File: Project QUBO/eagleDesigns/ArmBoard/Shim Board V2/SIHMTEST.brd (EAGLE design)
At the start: 71.1 x 81.3 mm, 30 parts, among them IC1 MCP2551/SN, U1 BME280

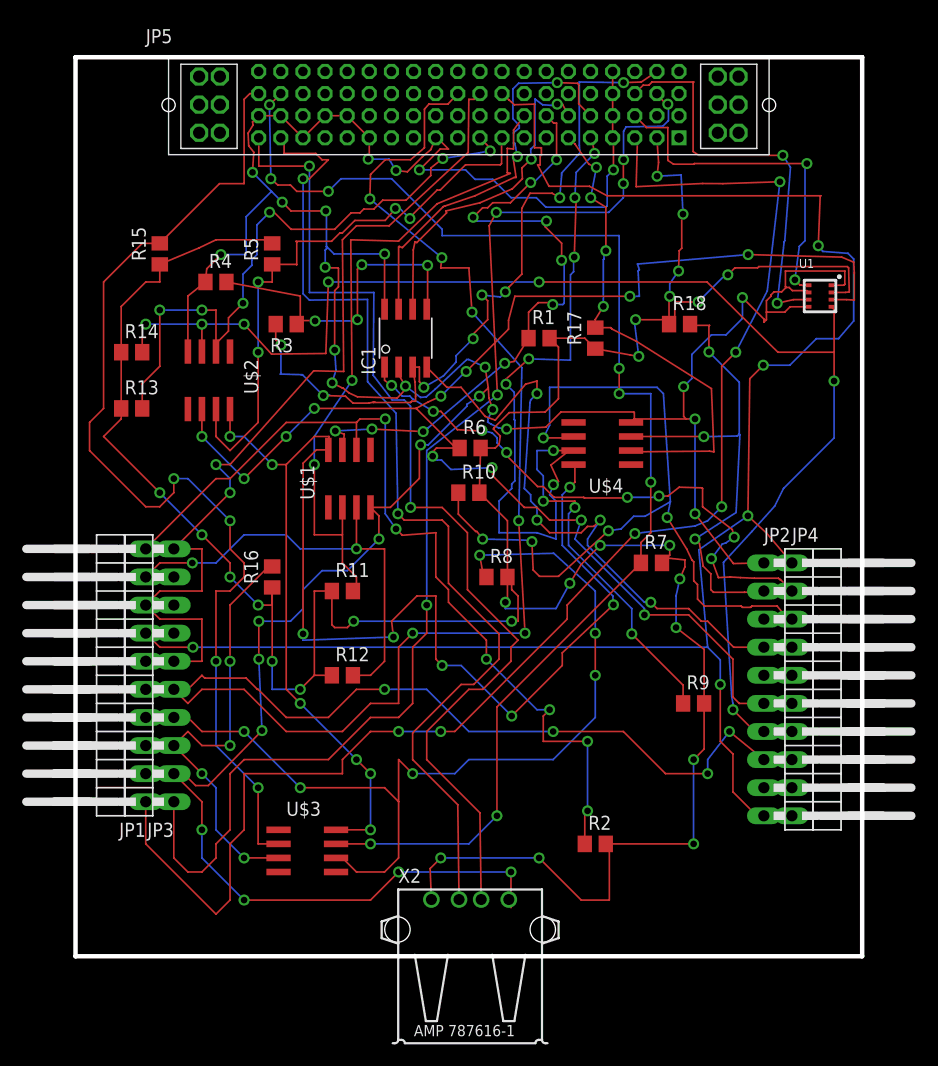
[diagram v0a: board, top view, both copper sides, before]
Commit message: 
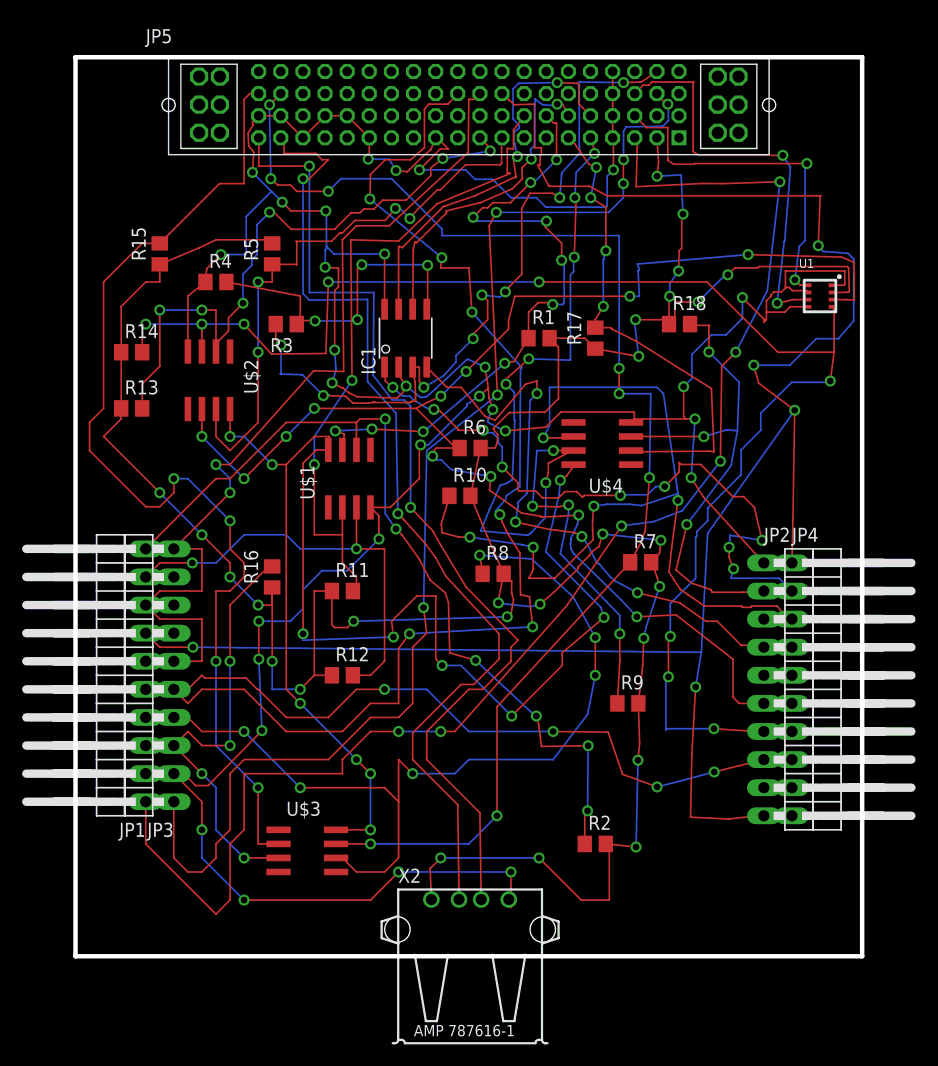
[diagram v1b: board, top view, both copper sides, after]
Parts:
- moved R9 5.94 mm to (49.9, 22.9)
- moved R7 0.97 mm to (51.1, 35.6)
- moved R10 0.85 mm to (34.8, 41.6)
- moved R8 0.45 mm to (37.8, 34.6)
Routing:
- net SPI_CLK: track 163.7 -> 177.7 mm
- net UNBUFFERSCL1: track 121.5 -> 132.8 mm, vias 7 -> 9
- net 5.0(BME): track 275.5 -> 265.0 mm
- net CANTX: track 52.5 -> 60.5 mm, vias 8 -> 9
- net UNBUFFERSDA3: track 74.3 -> 80.2 mm
- net UNBUFFERSDA2: track 84.8 -> 81.9 mm
- net BUFFERSDA3: track 91.4 -> 88.6 mm
- net UNBUFFERSDA0: track 80.5 -> 78.0 mm
- net CANRX: track 55.9 -> 53.5 mm
- net USB-: track 91.9 -> 89.5 mm
- net USB+: track 93.0 -> 90.9 mm
- net 3.3(1): track 129.2 -> 127.3 mm
- net GND: track 315.9 -> 314.4 mm
- net UNBUFFERSCL3: track 44.1 -> 44.9 mm
- net MISO: track 165.9 -> 166.7 mm
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
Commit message: 
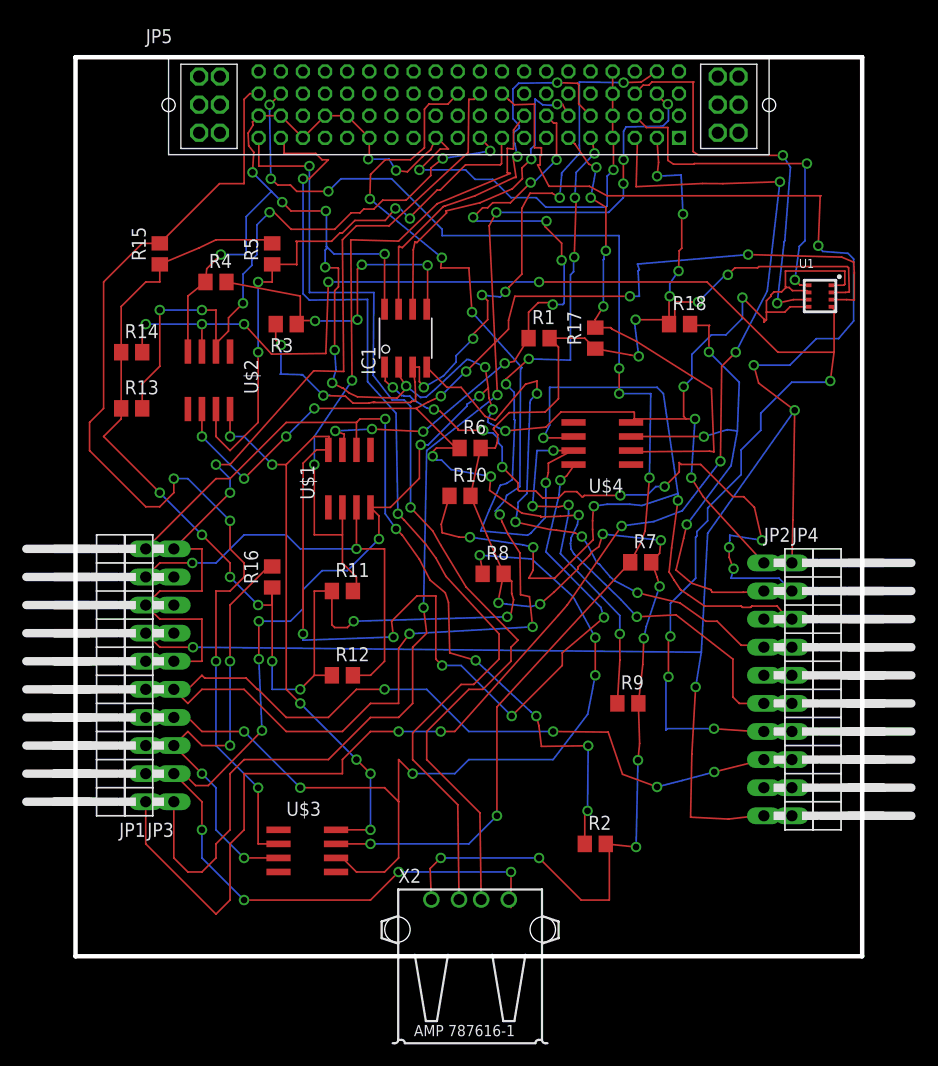
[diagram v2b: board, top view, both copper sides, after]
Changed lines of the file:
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@@
 </class>
 </classes>
-<designrules name="typical_4pcb">
+<designrules name="OshPark">
 <description language="de">&lt;b&gt;EAGLE Design Rules&lt;/b&gt;
 &lt;p&gt;
@@
 Einstellungen hier und speichern die Design Rules unter
 einem neuen Namen ab.</description>
-<description language="en">&lt;b&gt;EAGLE Design Rules&lt;/b&gt;
+<description language="en">&lt;b&gt;Laen's PCB Order Design Rules&lt;/b&gt;
 &lt;p&gt;
-The default Design Rules have been set to cover
-a wide range of applications. Your particular design
-may have different requirements, so please make the
-necessary adjustments and save your customized
-design rules under a new name.</description>
+Please make sure your boards conform to these design rules.</description>
 <param name="layerSetup" value="(1*16)"/>
-<param name="mtCopper" value="0.035559375mm 0.035559375mm 0.035559375mm 0.035559375mm 0.035559375mm 0.035559375mm 0.035559375mm 0.035559375mm 0.035559375mm 0.035559375mm 0.035559375mm 0.035559375mm 0.035559375mm 0.035559375mm 0.035559375mm 0.035559375mm"/>
-<param name="mtIsolate" value="1.501140625mm 0.149859375mm 0.200659375mm 0.149859375mm 0.200659375mm 0.149859375mm 0.200659375mm 0.149859375mm 0.200659375mm 0.149859375mm 0.200659375mm 0.149859375mm 0.200659375mm 0.149859375mm 0.200659375mm"/>
+<param name="mtCopper" value="0.0356mm 0.0356mm 0.0356mm 0.0356mm 0.0356mm 0.0356mm 0.0356mm 0.0356mm 0.0356mm 0.0356mm 0.0356mm 0.0356mm 0.0356mm 0.0356mm 0.0356mm 0.0356mm"/>
+<param name="mtIsolate" value="1.5011mm 0.1499mm 0.2007mm 0.1499mm 0.2007mm 0.1499mm 0.2007mm 0.1499mm 0.2007mm 0.1499mm 0.2007mm 0.1499mm 0.2007mm 0.1499mm 0.2007mm"/>
 <param name="mdWireWire" value="6mil"/>
 <param name="mdWirePad" value="6mil"/>
@@
 <param name="mnLayersViaInSmd" value="2"/>
 <param name="mdCopperDimension" value="15mil"/>
-<param name="mdDrill" value="8mil"/>
+<param name="mdDrill" value="6mil"/>
 <param name="mdSmdStop" value="0mil"/>
-<param name="msWidth" value="10mil"/>
-<param name="msDrill" value="15mil"/>
-<param name="msMicroVia" value="9.98981875mm"/>
+<param name="msWidth" value="6mil"/>
+<param name="msDrill" value="13mil"/>
+<param name="msMicroVia" value="13mil"/>
 <param name="msBlindViaRatio" value="0.5"/>
 <param name="rvPadTop" value="0.25"/>
@@
 <param name="rvMicroViaOuter" value="0.25"/>
 <param name="rvMicroViaInner" value="0.25"/>
-<param name="rlMinPadTop" value="10mil"/>
+<param name="rlMinPadTop" value="7mil"/>
 <param name="rlMaxPadTop" value="20mil"/>
-<param name="rlMinPadInner" value="10mil"/>
+<param name="rlMinPadInner" value="7mil"/>
 <param name="rlMaxPadInner" value="20mil"/>
-<param name="rlMinPadBottom" value="10mil"/>
+<param name="rlMinPadBottom" value="7mil"/>
 <param name="rlMaxPadBottom" value="20mil"/>
-<param name="rlMinViaOuter" value="8mil"/>
+<param name="rlMinViaOuter" value="7mil"/>
 <param name="rlMaxViaOuter" value="20mil"/>
-<param name="rlMinViaInner" value="8mil"/>
+<param name="rlMinViaInner" value="7mil"/>
 <param name="rlMaxViaInner" value="20mil"/>
 <param name="rlMinMicroViaOuter" value="4mil"/>
@@
 <param name="mvStopFrame" value="1"/>
 <param name="mvCreamFrame" value="0"/>
-<param name="mlMinStopFrame" value="4mil"/>
-<param name="mlMaxStopFrame" value="4mil"/>
+<param name="mlMinStopFrame" value="3mil"/>
+<param name="mlMaxStopFrame" value="3mil"/>
 <param name="mlMinCreamFrame" value="0mil"/>
 <param name="mlMaxCreamFrame" value="0mil"/>

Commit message: 
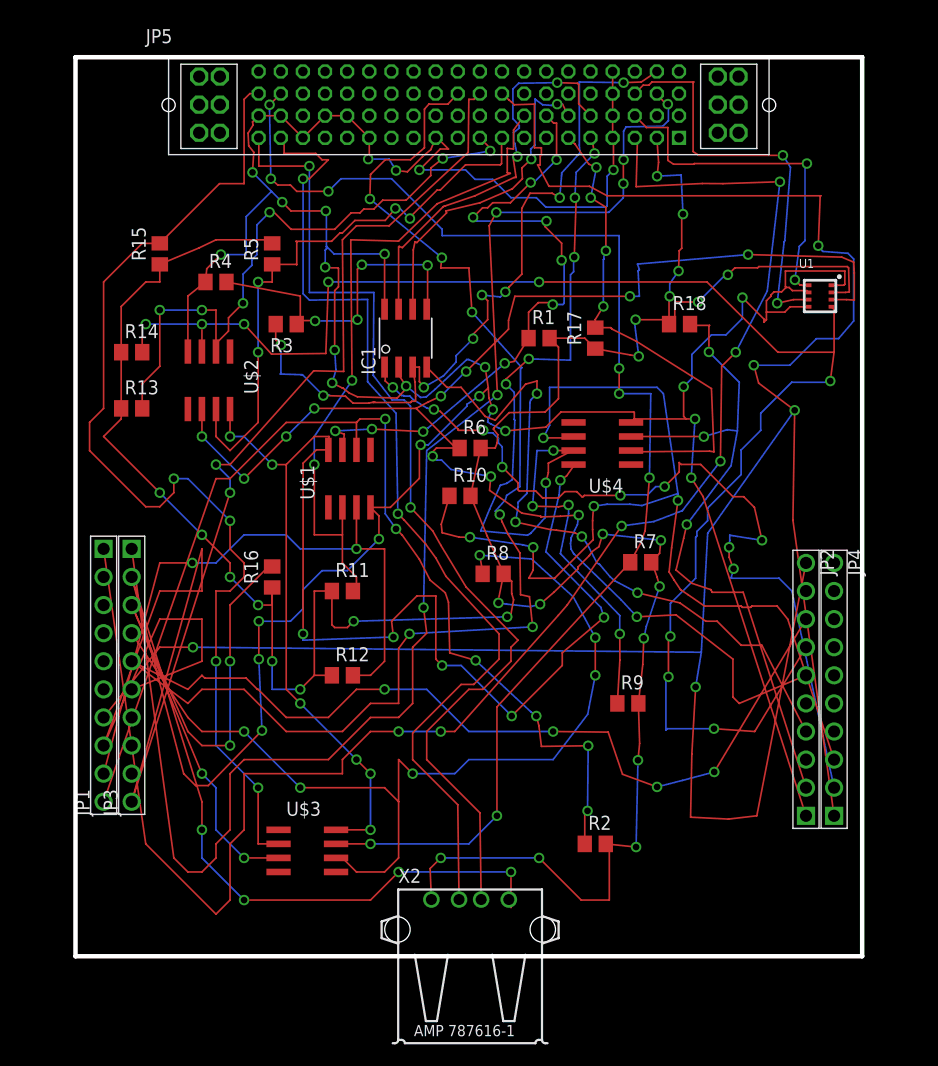
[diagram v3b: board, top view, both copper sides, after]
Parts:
- JP1, JP2, JP3, JP4: value (none) -> KK254_10-PIN; device pinhead:1X10/90 -> molex:KK254_10-PIN
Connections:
- net 3.3(1): now also JP1.P$1; no longer JP1.1
- net 5.0(3): now also JP3.P$1; no longer JP3.1
- net CANRX: now also JP2.P$4; no longer JP2.4
- net CANTX: now also JP4.P$2; no longer JP4.2
- net GND: now also JP2.P$1, JP3.P$2; no longer JP2.1, JP3.2
- net MISO: now also JP2.P$8, JP3.P$5; no longer JP2.8, JP3.5
- net MOSI: now also JP1.P$8, JP3.P$10, JP3.P$6; no longer JP1.8, JP3.10, JP3.6
- net PA3: now also JP2.P$9; no longer JP2.9
- net PB5: now also JP1.P$2; no longer JP1.2
- net PD6: now also JP4.P$8; no longer JP4.8
- net PD7: now also JP4.P$9; no longer JP4.9
- net PE2: now also JP3.P$8; no longer JP3.8
- net PE3: now also JP3.P$9; no longer JP3.9
- net PF4: now also JP4.P$10; no longer JP4.10
- net RES: now also JP2.P$5; no longer JP2.5
- net SPI_CLK: now also JP1.P$7, JP2.P$10, JP4.P$1; no longer JP1.7, JP2.10, JP4.1
- net U1RX(USB+)-: now also JP1.P$3; no longer JP1.3
- net U1TX(USB-)-: now also JP1.P$4; no longer JP1.4
- net U3RX-: now also JP4.P$6; no longer JP4.6
- net U3TX-: now also JP4.P$7; no longer JP4.7
- net U4RX-: now also JP4.P$4; no longer JP4.4
- net U4TX-: now also JP4.P$5; no longer JP4.5
- net U5RX-: now also JP1.P$5; no longer JP1.5
- net U5TX-: now also JP1.P$6; no longer JP1.6
- net U7RX-: now also JP2.P$3; no longer JP2.3
- net U7TX-: now also JP3.P$7; no longer JP3.7
- net UNBUFFERSCL0: now also JP1.P$9; no longer JP1.9
- net UNBUFFERSCL1: now also JP2.P$7; no longer JP2.7
- net UNBUFFERSCL2: now also JP3.P$3; no longer JP3.3
- net UNBUFFERSCL3: now also JP2.P$2; no longer JP2.2
- net UNBUFFERSDA0: now also JP1.P$10; no longer JP1.10
- net UNBUFFERSDA1: now also JP2.P$6; no longer JP2.6
- net UNBUFFERSDA2: now also JP3.P$4; no longer JP3.4
- net UNBUFFERSDA3: now also JP4.P$3; no longer JP4.3
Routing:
- net MOSI: track 81.9 -> 153.3 mm
- net GND: track 314.4 -> 371.8 mm
- net SPI_CLK: track 177.7 -> 229.8 mm
- net UNBUFFERSCL2: track 40.0 -> 63.6 mm
- net 3.3(1): track 127.3 -> 150.4 mm
- net 5.0(3): track 111.1 -> 134.2 mm
- net UNBUFFERSDA0: track 78.0 -> 99.9 mm
- net MISO: track 166.7 -> 187.1 mm
- net CANTX: track 60.5 -> 78.7 mm
- net UNBUFFERSCL0: track 41.0 -> 58.9 mm
- net UNBUFFERSCL3: track 44.9 -> 61.6 mm
- net UNBUFFERSDA3: track 80.2 -> 93.2 mm
- net CANRX: track 53.5 -> 62.0 mm
- net UNBUFFERSCL1: track 132.8 -> 140.9 mm
- net UNBUFFERSDA2: track 81.9 -> 89.8 mm
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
